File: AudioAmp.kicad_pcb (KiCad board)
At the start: 2 copper layers, 145 x 40 mm, 59 parts, among them Q1 MJE182G, Q12 MMBT5401, Q13 MMBT5401, Q2 MJE172G, Q3 MMBT5551(RANGE:200-300), Q9 MMBT5551(RANGE:200-300)

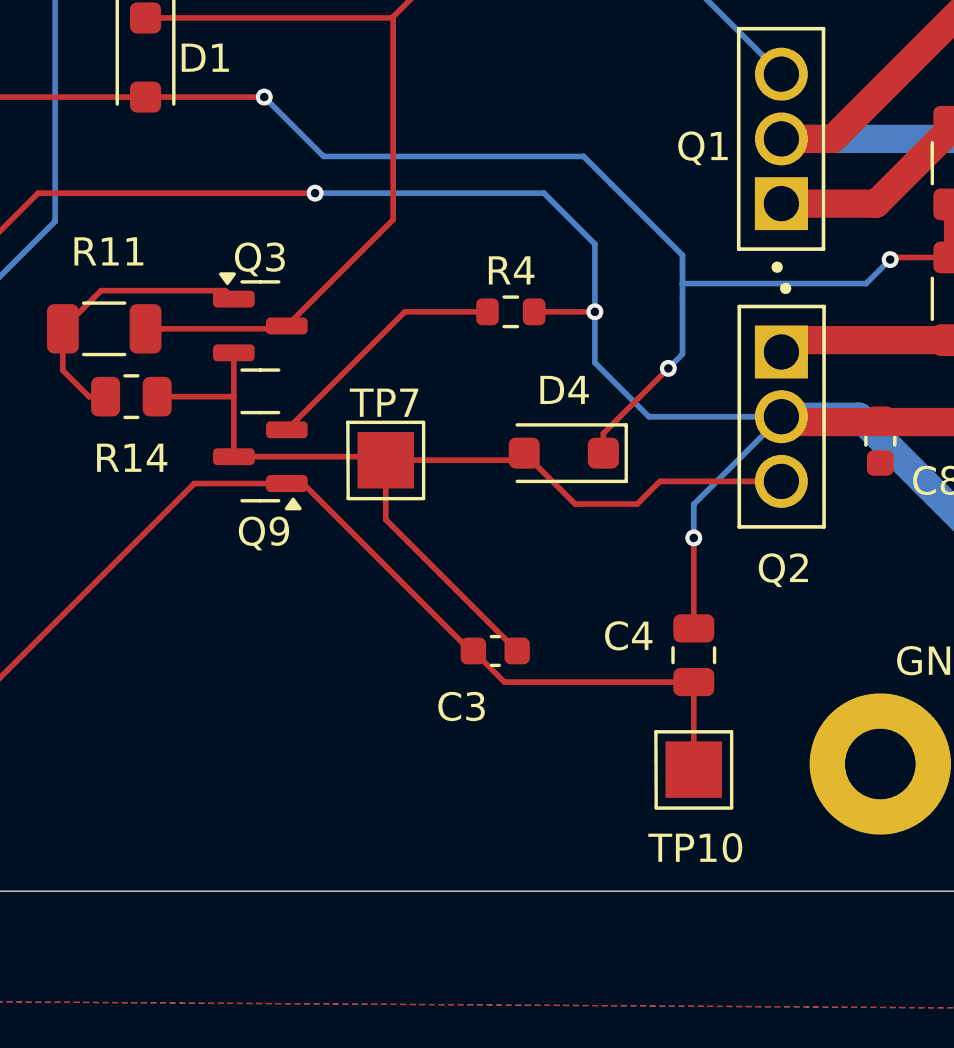
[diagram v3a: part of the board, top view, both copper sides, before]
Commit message: CHA: rev 1.2 - der C3 liegt falsch
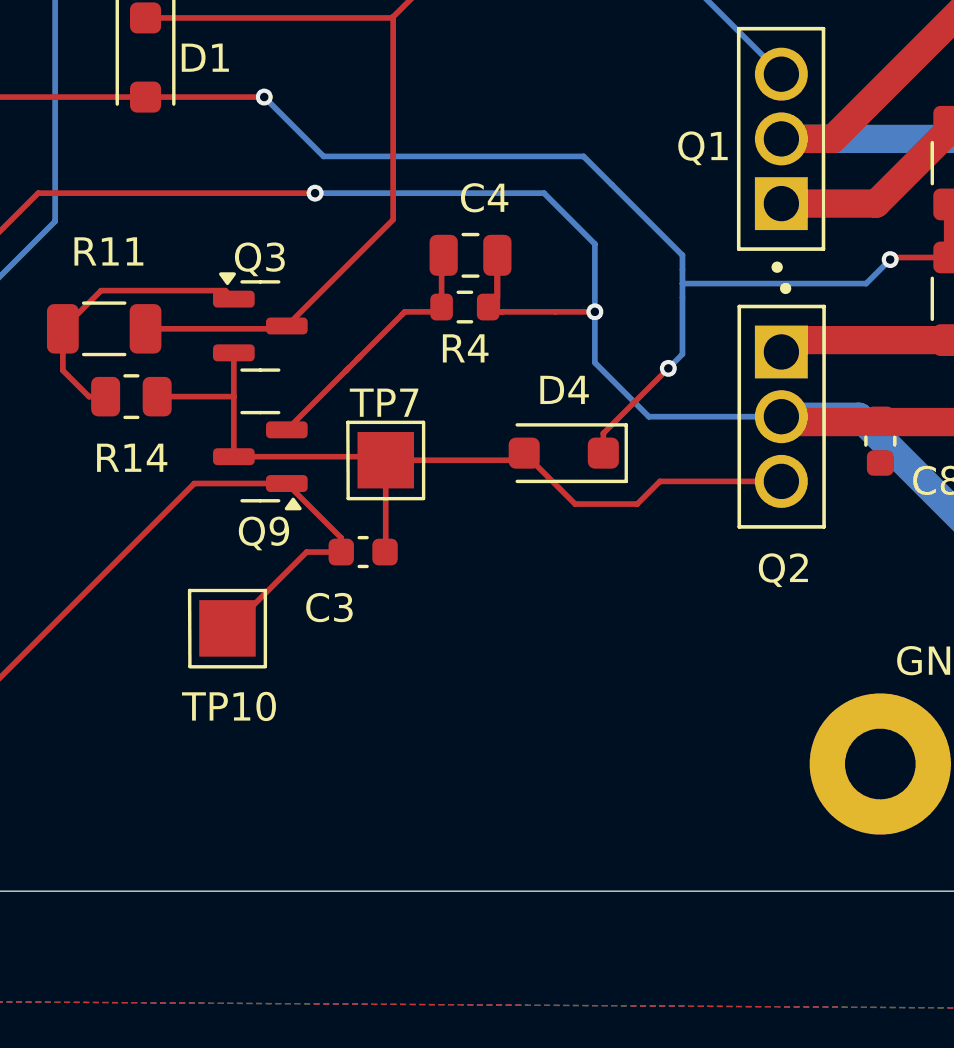
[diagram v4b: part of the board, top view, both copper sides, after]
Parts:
- moved TP10 17.2 mm to (134.9, 118.2)
- moved C4 16.2 mm to (143.5, 105.0), turned to 0 degrees
- moved C3 5.84 mm to (139.7, 115.5)
- moved R4 1.63 mm to (143.3, 106.8)
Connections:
- C4 pad 1: Net-(Q13-C) -> Net-(Q9-E)
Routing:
- net Net-(Q13-C): track 64.0 -> 52.5 mm
- net Net-(D4-A): track 35.7 -> 30.3 mm
- net Net-(D10-A): track 112.5 -> 108.3 mm, vias 3 -> 2
- net Net-(Q9-E): track 8.83 -> 10.1 mm
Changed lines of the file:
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@@
 	(footprint "TestPoint:TestPoint_Pad_2.0x2.0mm-breiter-silk"
 		(layer "F.Cu")
-		(at 151.4 123.2)
+		(at 134.9 118.2)
 		(descr "SMD rectangular pad as test Point, square 2.0mm side length")
 		(tags "test point SMD pad rectangle square")
@@
 	(footprint "Capacitor_SMD:C_0805_2012Metric"
 		(layer "F.Cu")
-		(at 151.4 119.15 90)
+		(at 143.5 105)
 		(descr "Capacitor SMD 0805 (2012 Metric), square (rectangular) end terminal, IPC-7351 nominal, (Body size source: IPC-SM-782 page 76, https://www.pcb-3d.com/wordpress/wp-content/uploads/ipc-sm-782a_amendment_1_and_2.pdf, https://docs.google.com/spreadsheets/d/1BsfQQcO9C6DZCsRaXUlFlo91Tg2WpOkGARC1WS5S8t0/edit?usp=sharing), generated with kicad-footprint-generator")
 		(tags "capacitor")
 		(property "Reference" "C4"
-			(at 0.65 -2.3 180)
+			(at 0.5 -2 0)
 			(layer "F.SilkS")
 			(effects
@@
 		)
 		(property "Value" "10n"
-			(at 0 1.68 90)
+			(at 0 1.68 0)
 			(layer "F.Fab")
 			(effects
@@
 		)
 		(property "Datasheet" "https://www.lcsc.com/datasheet/lcsc_datasheet_2304140030_Samsung-Electro-Mechanics-CL21B103KBANNNC_C1710.pdf"
-			(at 0 0 90)
+			(at 0 0 0)
 			(layer "F.Fab")
 			(hide yes)
@@
 		)
 		(property "Description" "50V 10nF X7R ±10% 0805 Multilayer Ceramic Capacitors MLCC - SMD/SMT ROHS"
-			(at 0 0 90)
+			(at 0 0 0)
 			(layer "F.Fab")
 			(hide yes)
@@
 		)
 		(property "MPN" "C1710"
-			(at 0 0 90)
+			(at 0 0 0)
 			(unlocked yes)
 			(layer "F.Fab")
@@
 		)
 		(fp_line
-			(start 1.7 -0.98)
-			(end 1.7 0.98)
+			(start -1.7 -0.98)
+			(end 1.7 -0.98)
 			(stroke
 				(width 0.05)
@@
 		)
 		(fp_line
-			(start -1.7 -0.98)
-			(end 1.7 -0.98)
+			(start -1.7 0.98)
+			(end -1.7 -0.98)
 			(stroke
 				(width 0.05)
@@
 		)
 		(fp_line
-			(start 1.7 0.98)
-			(end -1.7 0.98)
+			(start 1.7 -0.98)
+			(end 1.7 0.98)
 			(stroke
 				(width 0.05)
@@
 		)
 		(fp_line
-			(start -1.7 0.98)
-			(end -1.7 -0.98)
+			(start 1.7 0.98)
+			(end -1.7 0.98)
 			(stroke
 				(width 0.05)
@@
 		)
 		(fp_line
-			(start 1 -0.625)
-			(end 1 0.625)
+			(start -1 -0.625)
+			(end 1 -0.625)
 			(stroke
 				(width 0.1)
@@
 		)
 		(fp_line
-			(start -1 -0.625)
-			(end 1 -0.625)
+			(start -1 0.625)
+			(end -1 -0.625)
 			(stroke
 				(width 0.1)
@@
 		)
 		(fp_line
-			(start 1 0.625)
-			(end -1 0.625)
+			(start 1 -0.625)
+			(end 1 0.625)
 			(stroke
 				(width 0.1)
@@
 		)
 		(fp_line
-			(start -1 0.625)
-			(end -1 -0.625)
+			(start 1 0.625)
+			(end -1 0.625)
 			(stroke
 				(width 0.1)
@@
 		)
 		(fp_text user "${REFERENCE}"
-			(at 0 0 90)
+			(at 0 0 0)
 			(layer "F.Fab")
 			(effects
@@
 		)
 		(pad "1" smd roundrect
-			(at -0.95 0 90)
+			(at -0.95 0)
 			(size 1 1.45)
 			(layers "F.Cu" "F.Mask" "F.Paste")
 			(roundrect_rratio 0.25)
-			(net 5 "Net-(Q13-C)")
+			(net 22 "Net-(Q9-E)")
 			(pintype "passive")
 		)
 		(pad "2" smd roundrect
-			(at 0.95 0 90)
+			(at 0.95 0)
 			(size 1 1.45)
 			(layers "F.Cu" "F.Mask" "F.Paste")
@@
 	(footprint "Capacitor_SMD:C_0603_1608Metric"
 		(layer "F.Cu")
-		(at 144.375 119)
+		(at 139.7 115.5)
 		(descr "Capacitor SMD 0603 (1608 Metric), square (rectangular) end terminal, IPC-7351 nominal, (Body size source: IPC-SM-782 page 76, https://www.pcb-3d.com/wordpress/wp-content/uploads/ipc-sm-782a_amendment_1_and_2.pdf), generated with kicad-footprint-generator")
 		(tags "capacitor")
@@
 	(footprint "Resistor_SMD:R_0603_1608Metric"
 		(layer "F.Cu")
-		(at 144.925 107)
+		(at 143.3 106.83)
 		(descr "Resistor SMD 0603 (1608 Metric), square (rectangular) end terminal, IPC-7351 nominal, (Body size source: IPC-SM-782 page 72, https://www.pcb-3d.com/wordpress/wp-content/uploads/ipc-sm-782a_amendment_1_and_2.pdf), generated with kicad-footprint-generator")
 		(tags "resistor")
 		(property "Reference" "R4"
-			(at 0 -1.43 0)
+			(at 0 1.5 0)
 			(layer "F.SilkS")
 			(effects
@@
 	)
 	(segment
-		(start 143.5 119)
-		(end 137.575 113.075)
+		(start 138.925 115.5)
+		(end 137.7 115.5)
 		(width 0.2)
 		(layer "F.Cu")
@@
 	)
 	(segment
-		(start 143.6 119)
-		(end 143.5 119)
+		(start 137 113.075)
+		(end 138.925 115)
 		(width 0.2)
 		(layer "F.Cu")
@@
 	)
 	(segment
-		(start 117.575 123.575)
-		(end 117.575 115)
+		(start 135 118.2)
+		(end 134.9 118.2)
 		(width 0.2)
 		(layer "F.Cu")
@@
 	)
 	(segment
-		(start 151.4 120.1)
-		(end 151.4 123.2)
+		(start 117.575 123.575)
+		(end 117.575 115)
 		(width 0.2)
 		(layer "F.Cu")
@@
 	)
 	(segment
-		(start 144.7 120.1)
-		(end 151.4 120.1)
+		(start 133.725 113.075)
+		(end 122 124.8)
 		(width 0.2)
 		(layer "F.Cu")
@@
 	)
 	(segment
-		(start 133.725 113.075)
-		(end 122 124.8)
+		(start 137 113.075)
+		(end 133.725 113.075)
 		(width 0.2)
 		(layer "F.Cu")
@@
 	)
 	(segment
-		(start 143.6 119)
-		(end 144.7 120.1)
+		(start 138.925 115)
+		(end 138.925 115.5)
 		(width 0.2)
 		(layer "F.Cu")
@@
 	)
 	(segment
-		(start 137 113.075)
-		(end 133.725 113.075)
+		(start 137.7 115.5)
+		(end 135 118.2)
 		(width 0.2)
 		(layer "F.Cu")
@@
 	)
 	(segment
-		(start 145.15 119)
-		(end 140.5 114.35)
+		(start 140.5 115.475)
+		(end 140.475 115.5)
 		(width 0.2)
 		(layer "F.Cu")
@@
 	)
 	(segment
-		(start 145.4 112)
-		(end 147.2 113.8)
+		(start 140.5 112.25)
+		(end 140.5 115.475)
 		(width 0.2)
 		(layer "F.Cu")
@@
 	)
 	(segment
-		(start 140.5 114.35)
-		(end 140.5 112.25)
+		(start 145.4 112)
+		(end 147.2 113.8)
 		(width 0.2)
 		(layer "F.Cu")
@@
 	)
 	(segment
-		(start 145.75 107)
+		(start 146.5 107)
 		(end 147.9 107)
 		(width 0.2)
@@
 	)
 	(segment
+		(start 144.6 107)
+		(end 144.325 107)
+		(width 0.2)
+		(layer "F.Cu")
+		(net 7)
+	)
+	(segment
 		(start 124 107)
 		(end 128.2 102.8)
@@
 	)
 	(segment
-		(start 151.4 118.2)
-		(end 151.4 115)
-		(width 0.2)
-		(layer "F.Cu")
-		(net 7)
-	)
-	(segment
 		(start 120.5 120.5)
 		(end 120.5 116.75)
@@
 	)
 	(segment
-		(start 145.75 107)
-		(end 145.75 107.25)
-		(width 0.2)
-		(layer "F.Cu")
-		(net 7)
-	)
-	(segment
 		(start 128.2 102.8)
 		(end 138 102.8)
@@
 	)
 	(segment
+		(start 146.5 107)
+		(end 144.6 107)
+		(width 0.2)
+		(layer "F.Cu")
+		(net 7)
+	)
+	(segment
 		(start 166.624 110.9)
 		(end 154.69 110.9)
@@
 		(net 7)
 	)
-	(via
-		(at 151.4 115)
-		(size 0.6)
-		(drill 0.3)
-		(layers "F.Cu" "B.Cu")
+	(segment
+		(start 144.45 105)
+		(end 144.45 106.85)
+		(width 0.2)
+		(layer "F.Cu")
+		(net 7)
+	)
+	(segment
+		(start 144.45 105)
+		(end 144.45 106.505)
+		(width 0.2)
+		(layer "F.Cu")
 		(net 7)
 	)
@@
 	)
 	(segment
-		(start 151.4 113.81)
-		(end 154.5 110.71)
-		(width 0.2)
-		(layer "B.Cu")
-		(net 7)
-	)
-	(segment
-		(start 151.4 115)
-		(end 151.4 113.81)
-		(width 0.2)
-		(layer "B.Cu")
-		(net 7)
-	)
-	(segment
 		(start 166 119.464467)
 		(end 157.245533 110.71)
@@
 	)
 	(segment
-		(start 141.175 107)
-		(end 144.1 107)
+		(start 142.475 105.075)
+		(end 142.55 105)
+		(width 0.2)
+		(layer "F.Cu")
+		(net 22)
+	)
+	(segment
+		(start 139.0875 109.0875)
+		(end 139.5875 108.5875)
 		(width 0.2)
 		(layer "F.Cu")
@@
 	(segment
 		(start 137 111.175)
+		(end 139.0875 109.0875)
+		(width 0.2)
+		(layer "F.Cu")
+		(net 22)
+	)
+	(segment
+		(start 142.55 105.625)
+		(end 142.55 105)
+		(width 0.2)
+		(layer "F.Cu")
+		(net 22)
+	)
+	(segment
+		(start 142.475 106.83)
+		(end 142.475 105.075)
+		(width 0.2)
+		(layer "F.Cu")
+		(net 22)
+	)
+	(segment
+		(start 141.175 107)
+		(end 141.0875 107.0875)
+		(width 0.2)
+		(layer "F.Cu")
+		(net 22)
+	)
+	(segment
+		(start 142.675 107)
 		(end 141.175 107)
 		(width 0.2)
 		(layer "F.Cu")
+		(net 22)
+	)
+	(segment
+		(start 139.5875 108.5875)
+		(end 141.0875 107.0875)
+		(width 0.2)
+		(layer "F.Cu")
+		(net 22)
+	)
+	(segment
+		(start 139.175 109)
+		(end 139.0875 109.0875)
+		(width 0.2)
+		(layer "F.Cu")
+		(net 22)
+	)
+	(segment
+		(start 139.5875 108.5875)
+		(end 139.5 108.675)
+		(width 0.2)
+		(layer "F.Cu")
